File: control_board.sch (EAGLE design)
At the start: 47 parts, among them IC1 4021N, J1 AUDIO_JACK_3.5MM_KIT, Y1 16MHz

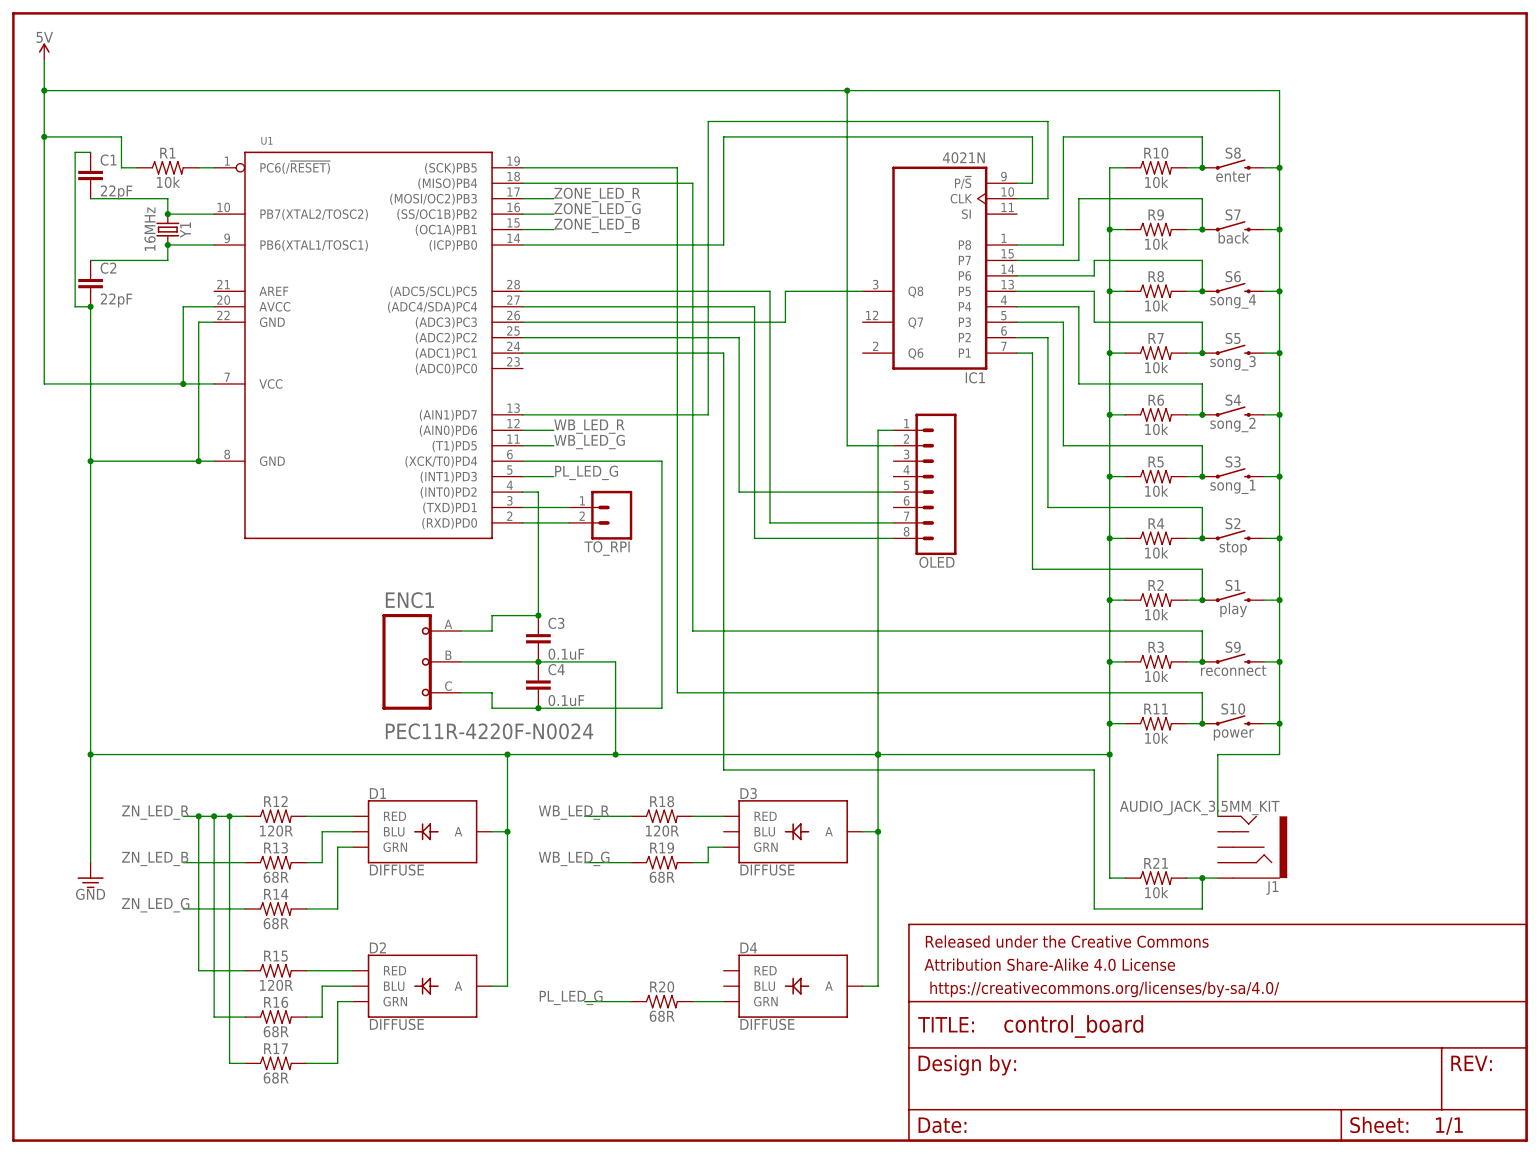
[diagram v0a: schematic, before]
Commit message: Use Teensy LC rather than ATMEGA328
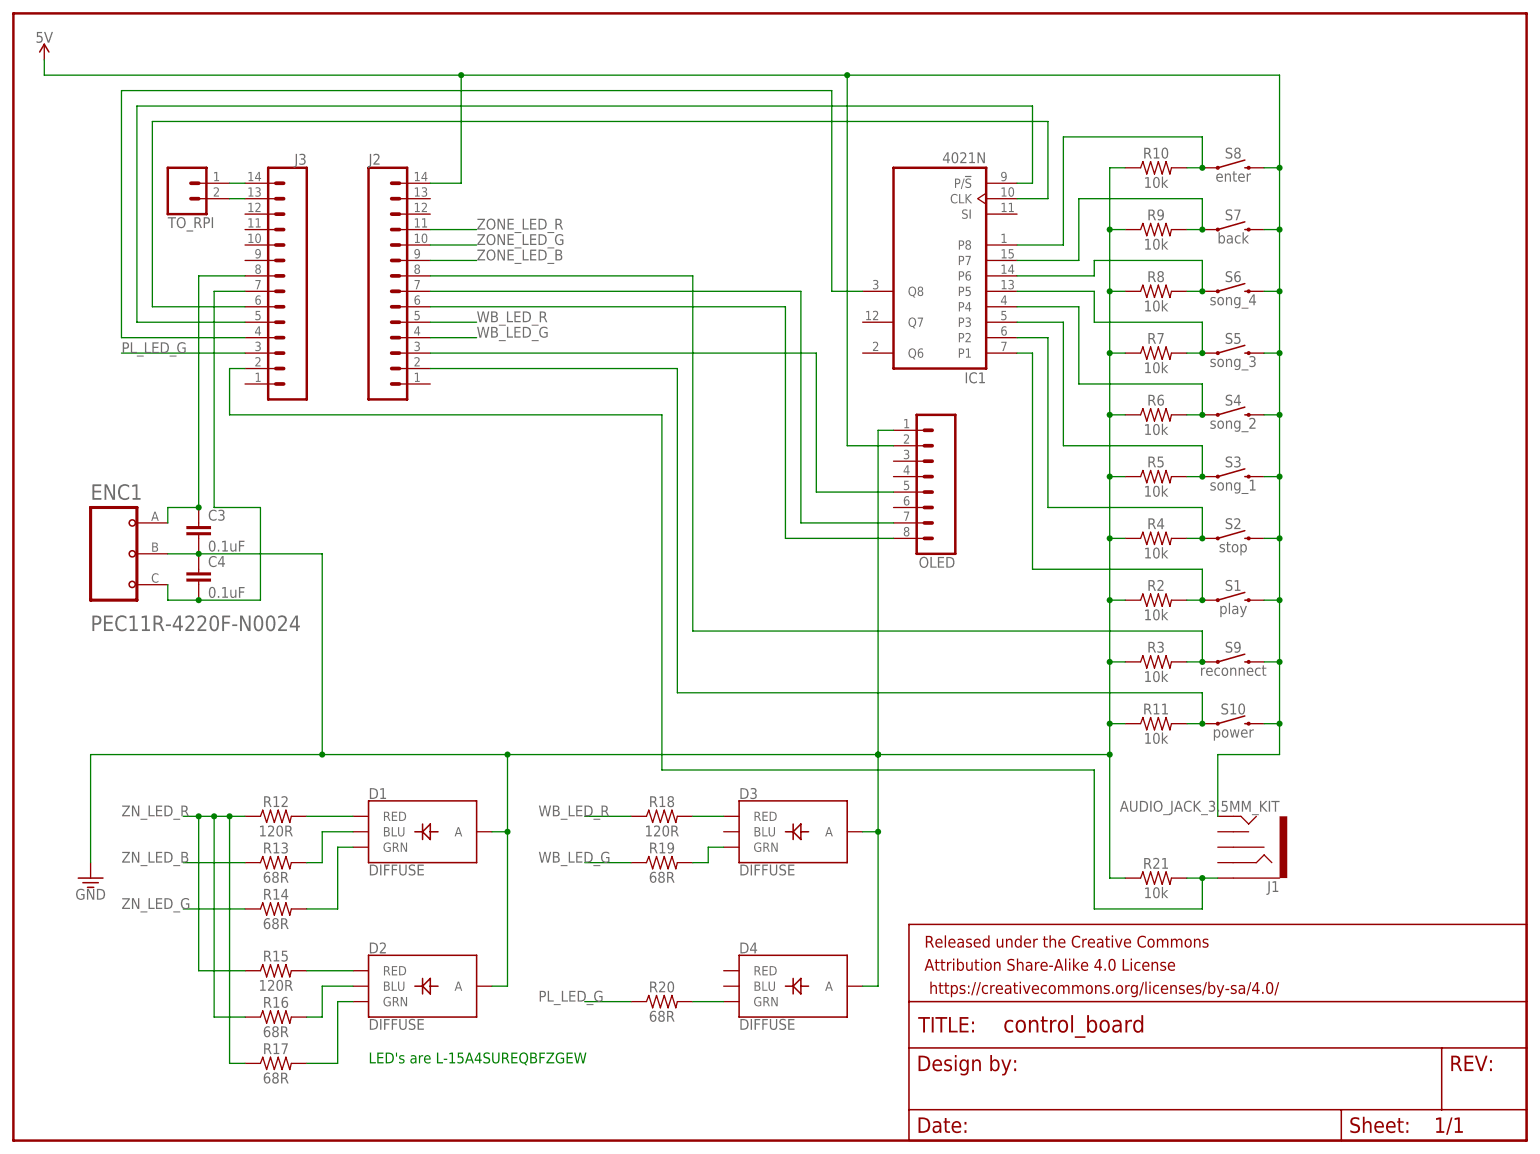
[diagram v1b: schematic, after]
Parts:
- removed C1, C2: 22pF, SparkFun-Capacitors:22PF-PTH-2.54MM-200V-5%
- removed R1: 10k, SparkFun-Resistors:10KOHM-HORIZ-1/4W-1%
- removed U1: (no value), Seeed-IC:MCU-ATMEGA328P-PU(DIP28)
- removed Y1: 16MHz, SparkFun-Clocks:CRYSTAL-16MHZPTH-HC49US
- added J2, J3: (no value), SparkFun-Connectors:CONN_14
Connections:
- removed net N$29: OLED.8, U1.(ADC4/SDA)PC4
- removed net N$32: TO_RPI.1, U1.(TXD)PD1
- removed net N$33: TO_RPI.2, U1.(RXD)PD0
- net 3.3V: no longer C1.1, C2.2, U1.GND, U1.GND@1
- net 5V: now also J2.14; no longer R1.1, U1.AVCC, U1.VCC@1
- net N$1: now also IC1A.Q8, J3.4; no longer C1.2, U1.PB7(XTAL2/TOSC2), Y1.1
- net N$14: now also J3.2; no longer U1.(ADC1)PC1
- net N$19: now also J3.8; no longer U1.(INT0)PD2
- net N$2: now also J3.14, TO_RPI.1; no longer C2.1, U1.PB6(XTAL1/TOSC1), Y1.2
- net N$20: now also J3.7; no longer U1.(XCK/T0)PD4
- net N$21: now also J2.8; no longer U1.(MISO)PB4
- net N$22: now also J2.2; no longer U1.(SCK)PB5
- net N$3: now also J3.13, TO_RPI.2; no longer R1.2, U1.PC6(/!RESET)
- net N$30: now also J2.7; no longer U1.(ADC5/SCL)PC5
- net N$31: now also J2.3; no longer U1.(ADC2)PC2
- net N$4: now also IC1A.CLK, J3.6; no longer IC1A.Q8, U1.(ADC3)PC3
- net N$8: now also IC1A.P/!S, J3.5; no longer IC1A.CLK, U1.(AIN1)PD7
- net N$9: now also J2.6, OLED.8; no longer IC1A.P/!S, U1.(ICP)PB0
- net PL_LED_G: now also J3.3; no longer U1.(INT1)PD3
- net WB_LED_G: now also J2.4; no longer U1.(T1)PD5
- net WB_LED_R: now also J2.5; no longer U1.(AIN0)PD6
- net ZONE_LED_B: now also J2.9; no longer U1.(OC1A)PB1
- net ZONE_LED_G: now also J2.10; no longer U1.(SS/OC1B)PB2
- net ZONE_LED_R: now also J2.11; no longer U1.(MOSI/OC2)PB3
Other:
- note added: "LED's are L-15A4SUREQBFZGEW"
- moved on the sheet: C3, C4, ENC1, TO_RPI

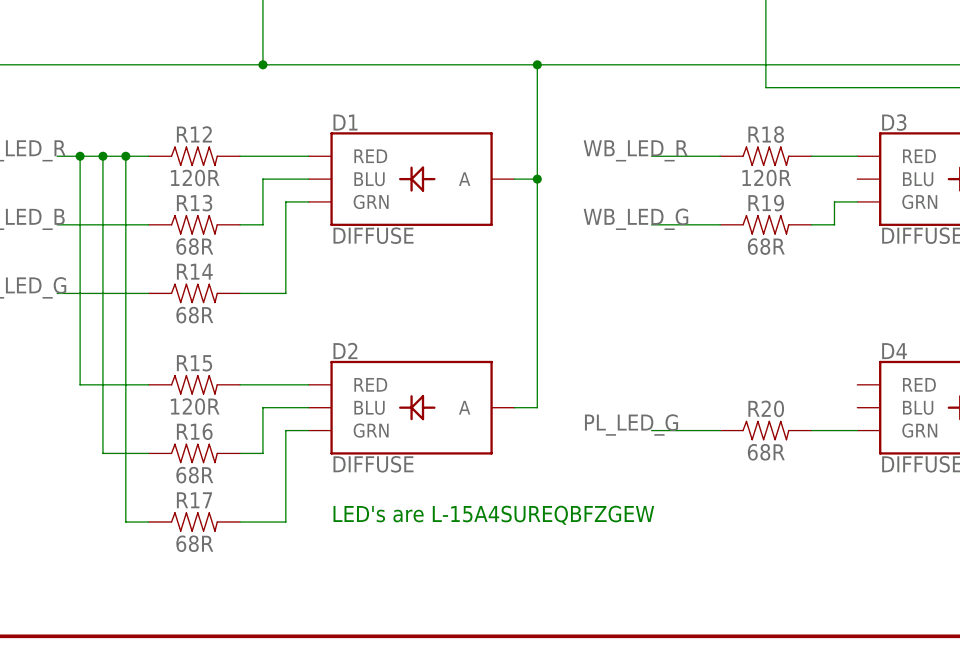
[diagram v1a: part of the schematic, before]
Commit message: Change LED resistor values.
helps keep LEDs lit at a consistent brightness.
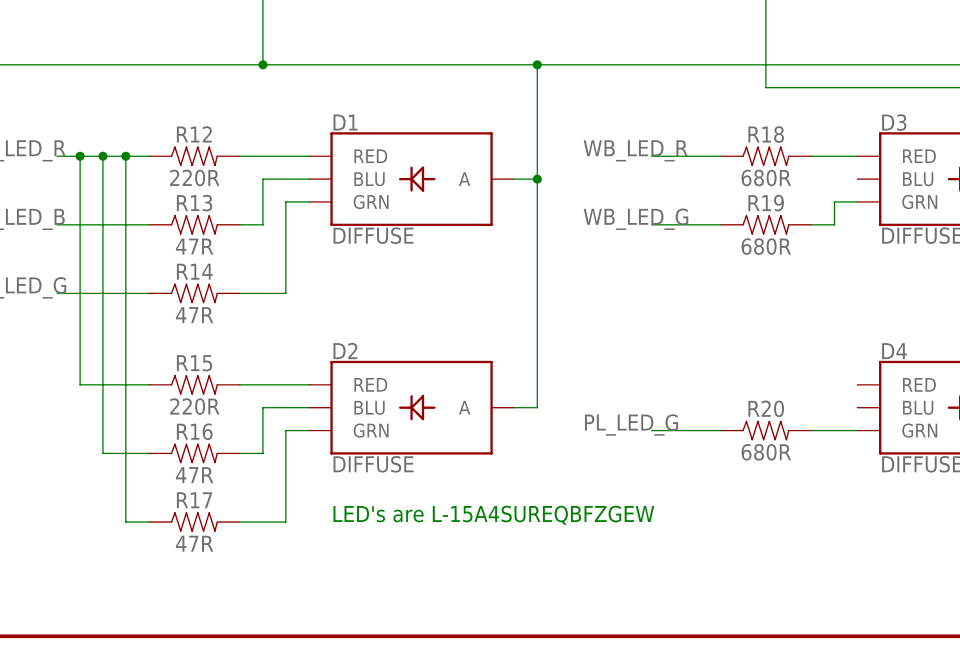
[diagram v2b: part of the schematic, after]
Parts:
- R12, R15: value 120R -> 220R
- R13, R14, R16, R17: value 68R -> 47R
- R18: value 120R -> 680R
- R19, R20: value 68R -> 680R
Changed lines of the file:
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@@
 <part name="D1" library="SparkFun-LED" library_urn="urn:adsk.eagle:library:529" deviceset="LED-RGB-CA" device="DIFFUSE" package3d_urn="urn:adsk.eagle:package:39368/1" value="DIFFUSE"/>
 <part name="D2" library="SparkFun-LED" library_urn="urn:adsk.eagle:library:529" deviceset="LED-RGB-CA" device="DIFFUSE" package3d_urn="urn:adsk.eagle:package:39368/1" value="DIFFUSE"/>
-<part name="R12" library="SparkFun-Resistors" library_urn="urn:adsk.eagle:library:532" deviceset="100OHM" device="-HORIZ-1/4W-1%" package3d_urn="urn:adsk.eagle:package:39658/1" value="120R"/>
-<part name="R13" library="SparkFun-Resistors" library_urn="urn:adsk.eagle:library:532" deviceset="100OHM" device="-HORIZ-1/4W-1%" package3d_urn="urn:adsk.eagle:package:39658/1" value="68R"/>
-<part name="R14" library="SparkFun-Resistors" library_urn="urn:adsk.eagle:library:532" deviceset="100OHM" device="-HORIZ-1/4W-1%" package3d_urn="urn:adsk.eagle:package:39658/1" value="68R"/>
-<part name="R15" library="SparkFun-Resistors" library_urn="urn:adsk.eagle:library:532" deviceset="100OHM" device="-HORIZ-1/4W-1%" package3d_urn="urn:adsk.eagle:package:39658/1" value="120R"/>
-<part name="R16" library="SparkFun-Resistors" library_urn="urn:adsk.eagle:library:532" deviceset="100OHM" device="-HORIZ-1/4W-1%" package3d_urn="urn:adsk.eagle:package:39658/1" value="68R"/>
-<part name="R17" library="SparkFun-Resistors" library_urn="urn:adsk.eagle:library:532" deviceset="100OHM" device="-HORIZ-1/4W-1%" package3d_urn="urn:adsk.eagle:package:39658/1" value="68R"/>
+<part name="R12" library="SparkFun-Resistors" library_urn="urn:adsk.eagle:library:532" deviceset="100OHM" device="-HORIZ-1/4W-1%" package3d_urn="urn:adsk.eagle:package:39658/1" value="220R"/>
+<part name="R13" library="SparkFun-Resistors" library_urn="urn:adsk.eagle:library:532" deviceset="100OHM" device="-HORIZ-1/4W-1%" package3d_urn="urn:adsk.eagle:package:39658/1" value="47R"/>
+<part name="R14" library="SparkFun-Resistors" library_urn="urn:adsk.eagle:library:532" deviceset="100OHM" device="-HORIZ-1/4W-1%" package3d_urn="urn:adsk.eagle:package:39658/1" value="47R"/>
+<part name="R15" library="SparkFun-Resistors" library_urn="urn:adsk.eagle:library:532" deviceset="100OHM" device="-HORIZ-1/4W-1%" package3d_urn="urn:adsk.eagle:package:39658/1" value="220R"/>
+<part name="R16" library="SparkFun-Resistors" library_urn="urn:adsk.eagle:library:532" deviceset="100OHM" device="-HORIZ-1/4W-1%" package3d_urn="urn:adsk.eagle:package:39658/1" value="47R"/>
+<part name="R17" library="SparkFun-Resistors" library_urn="urn:adsk.eagle:library:532" deviceset="100OHM" device="-HORIZ-1/4W-1%" package3d_urn="urn:adsk.eagle:package:39658/1" value="47R"/>
 <part name="D3" library="SparkFun-LED" library_urn="urn:adsk.eagle:library:529" deviceset="LED-RGB-CA" device="DIFFUSE" package3d_urn="urn:adsk.eagle:package:39368/1" value="DIFFUSE"/>
-<part name="R18" library="SparkFun-Resistors" library_urn="urn:adsk.eagle:library:532" deviceset="100OHM" device="-HORIZ-1/4W-1%" package3d_urn="urn:adsk.eagle:package:39658/1" value="120R"/>
-<part name="R19" library="SparkFun-Resistors" library_urn="urn:adsk.eagle:library:532" deviceset="100OHM" device="-HORIZ-1/4W-1%" package3d_urn="urn:adsk.eagle:package:39658/1" value="68R"/>
+<part name="R18" library="SparkFun-Resistors" library_urn="urn:adsk.eagle:library:532" deviceset="100OHM" device="-HORIZ-1/4W-1%" package3d_urn="urn:adsk.eagle:package:39658/1" value="680R"/>
+<part name="R19" library="SparkFun-Resistors" library_urn="urn:adsk.eagle:library:532" deviceset="100OHM" device="-HORIZ-1/4W-1%" package3d_urn="urn:adsk.eagle:package:39658/1" value="680R"/>
 <part name="D4" library="SparkFun-LED" library_urn="urn:adsk.eagle:library:529" deviceset="LED-RGB-CA" device="DIFFUSE" package3d_urn="urn:adsk.eagle:package:39368/1" value="DIFFUSE"/>
-<part name="R20" library="SparkFun-Resistors" library_urn="urn:adsk.eagle:library:532" deviceset="100OHM" device="-HORIZ-1/4W-1%" package3d_urn="urn:adsk.eagle:package:39658/1" value="68R"/>
+<part name="R20" library="SparkFun-Resistors" library_urn="urn:adsk.eagle:library:532" deviceset="100OHM" device="-HORIZ-1/4W-1%" package3d_urn="urn:adsk.eagle:package:39658/1" value="680R"/>
 <part name="OLED" library="SparkFun-Connectors" library_urn="urn:adsk.eagle:library:513" deviceset="CONN_08" device="&quot;" package3d_urn="urn:adsk.eagle:package:38138/1"/>
 <part name="TO_RPI" library="SparkFun-Connectors" library_urn="urn:adsk.eagle:library:513" deviceset="CONN_02" device="" package3d_urn="urn:adsk.eagle:package:38039/1"/>
